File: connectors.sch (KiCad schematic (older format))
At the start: 43 parts, among them J11 20021121-00010C4LF, J12 70543-0001, J13 70543-0001, J14 70543-0001, J15 70543-0001, J16 70543-0001, J17 70543-0001, J18 70543-0001, J19 70543-0001, J20 70543-0003, J21 70543-0002, J22 70543-0002, J23 70543-0002, J24 Conn_02x20_Odd_Even

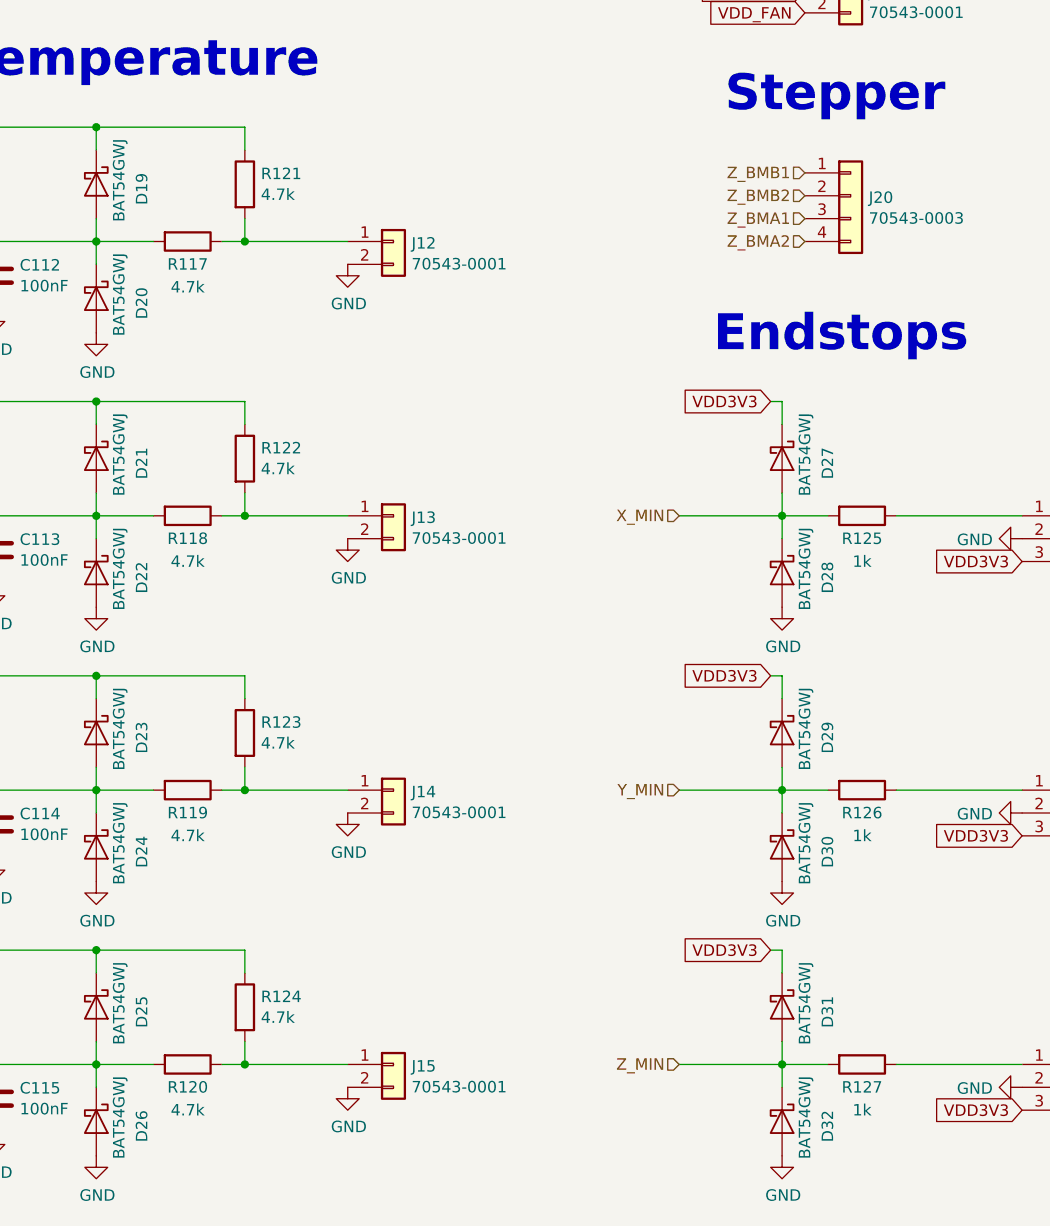
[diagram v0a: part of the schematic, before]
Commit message: Add transistor for boot selection
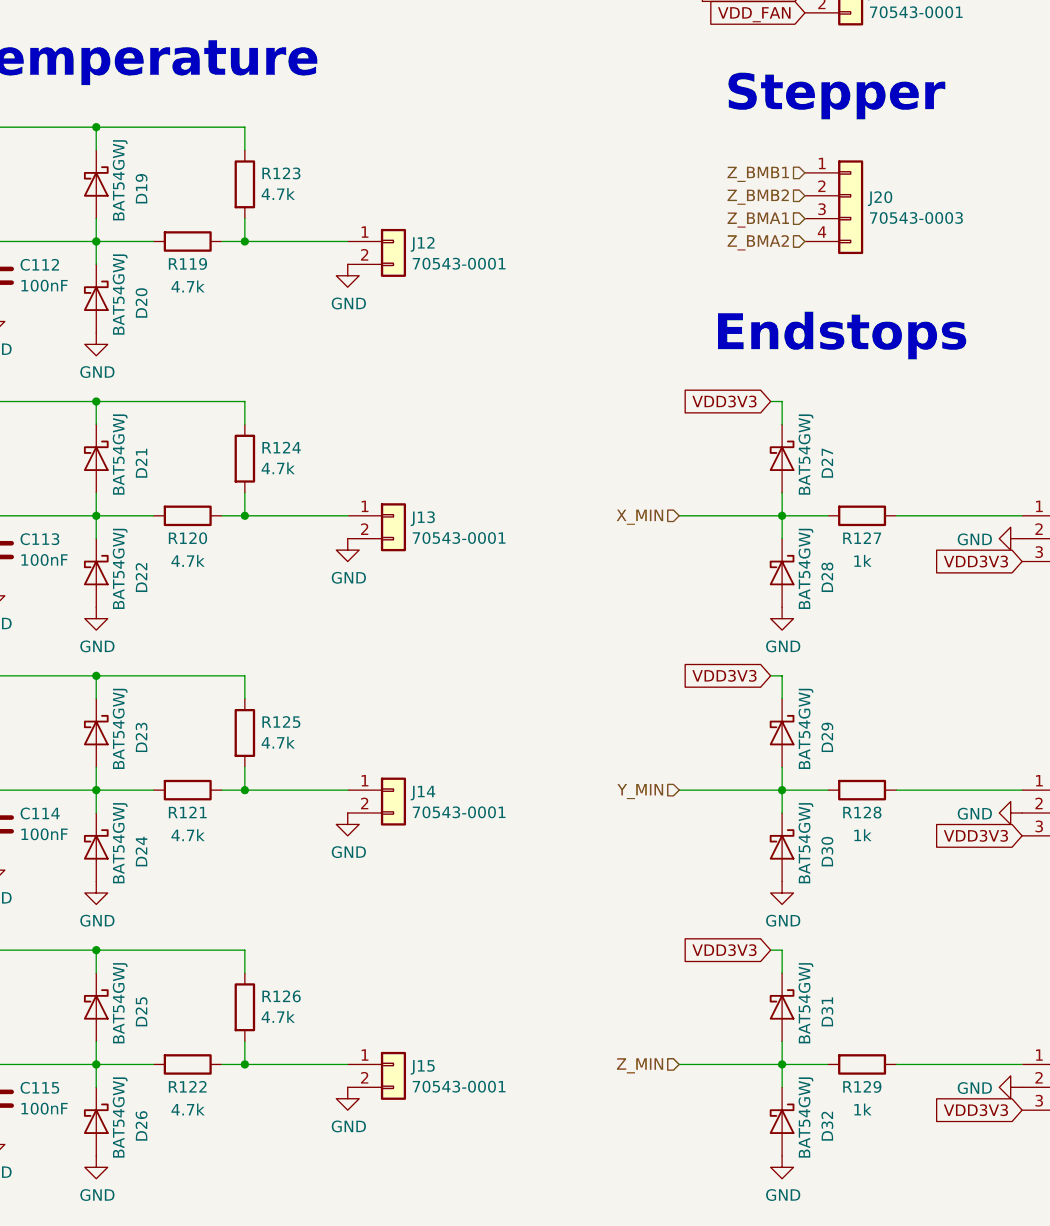
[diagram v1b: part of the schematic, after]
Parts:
- renumbered R117 to R119, R118 to R120, R119 to R121, R120 to R122, R121 to R123, R122 to R124, R123 to R125, R124 to R126, R125 to R127, R126 to R128, R127 to R129
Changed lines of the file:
@@
 TEMP1
 $Comp
-L Device:R R117
+L Device:R R119
 U 1 1 5B1719A1
 P 1900 3300
-F 0 "R117" V 2000 3300 50  0000 C CNN
+F 0 "R119" V 2000 3300 50  0000 C CNN
 F 1 "4.7k" V 2100 3300 50  0000 C CNN
 F 2 "Resistor_SMD:R_0603_1608Metric" V 1830 3300 50  0001 C CNN
@@
 $EndComp
 $Comp
-L Device:R R121
+L Device:R R123
 U 1 1 5B1719A8
 P 2150 3050
-F 0 "R121" H 2220 3096 50  0000 L CNN
+F 0 "R123" H 2220 3096 50  0000 L CNN
 F 1 "4.7k" H 2220 3005 50  0000 L CNN
 F 2 "Resistor_SMD:R_0603_1608Metric" V 2080 3050 50  0001 C CNN
@@
 VDD_FAN
 $Comp
-L Device:R R125
+L Device:R R127
 U 1 1 5B40FD8A
 P 4850 4500
-F 0 "R125" V 4950 4500 50  0000 C CNN
+F 0 "R127" V 4950 4500 50  0000 C CNN
 F 1 "1k" V 5050 4500 50  0000 C CNN
 F 2 "Resistor_SMD:R_0603_1608Metric" V 4780 4500 50  0001 C CNN
@@
 	4500 4500 4700 4500
 $Comp
-L Device:R R126
+L Device:R R128
 U 1 1 5B453619
 P 4850 5700
-F 0 "R126" V 4950 5700 50  0000 C CNN
+F 0 "R128" V 4950 5700 50  0000 C CNN
 F 1 "1k" V 5050 5700 50  0000 C CNN
 F 2 "Resistor_SMD:R_0603_1608Metric" V 4780 5700 50  0001 C CNN
@@
 	4500 5700 4700 5700
 $Comp
-L Device:R R127
+L Device:R R129
 U 1 1 5B45771E
 P 4850 6900
-F 0 "R127" V 4950 6900 50  0000 C CNN
+F 0 "R129" V 4950 6900 50  0000 C CNN
 F 1 "1k" V 5050 6900 50  0000 C CNN
 F 2 "Resistor_SMD:R_0603_1608Metric" V 4780 6900 50  0001 C CNN
@@
 Connection ~ 2150 3300
 $Comp
-L Device:R R118
+L Device:R R120
 U 1 1 5B5657F4
 P 1900 4500
-F 0 "R118" V 2000 4500 50  0000 C CNN
+F 0 "R120" V 2000 4500 50  0000 C CNN
 F 1 "4.7k" V 2100 4500 50  0000 C CNN
 F 2 "Resistor_SMD:R_0603_1608Metric" V 1830 4500 50  0001 C CNN
@@
 $EndComp
 $Comp
-L Device:R R122
+L Device:R R124
 U 1 1 5B5657FB
 P 2150 4250
-F 0 "R122" H 2220 4296 50  0000 L CNN
+F 0 "R124" H 2220 4296 50  0000 L CNN
 F 1 "4.7k" H 2220 4205 50  0000 L CNN
 F 2 "Resistor_SMD:R_0603_1608Metric" V 2080 4250 50  0001 C CNN
@@
 Connection ~ 2150 4500
 $Comp
-L Device:R R119
+L Device:R R121
 U 1 1 5B57C5BA
 P 1900 5700
-F 0 "R119" V 2000 5700 50  0000 C CNN
+F 0 "R121" V 2000 5700 50  0000 C CNN
 F 1 "4.7k" V 2100 5700 50  0000 C CNN
 F 2 "Resistor_SMD:R_0603_1608Metric" V 1830 5700 50  0001 C CNN
@@
 $EndComp
 $Comp
-L Device:R R123
+L Device:R R125
 U 1 1 5B57C5C1
 P 2150 5450
-F 0 "R123" H 2220 5496 50  0000 L CNN
+F 0 "R125" H 2220 5496 50  0000 L CNN
 F 1 "4.7k" H 2220 5405 50  0000 L CNN
 F 2 "Resistor_SMD:R_0603_1608Metric" V 2080 5450 50  0001 C CNN
@@
 $EndComp
 $Comp
-L Device:R R120
+L Device:R R122
 U 1 1 5BC983A7
 P 1900 6900
-F 0 "R120" V 2000 6900 50  0000 C CNN
+F 0 "R122" V 2000 6900 50  0000 C CNN
 F 1 "4.7k" V 2100 6900 50  0000 C CNN
 F 2 "Resistor_SMD:R_0603_1608Metric" V 1830 6900 50  0001 C CNN
@@
 $EndComp
 $Comp
-L Device:R R124
+L Device:R R126
 U 1 1 5BC983AE
 P 2150 6650
-F 0 "R124" H 2220 6696 50  0000 L CNN
+F 0 "R126" H 2220 6696 50  0000 L CNN
 F 1 "4.7k" H 2220 6605 50  0000 L CNN
 F 2 "Resistor_SMD:R_0603_1608Metric" V 2080 6650 50  0001 C CNN

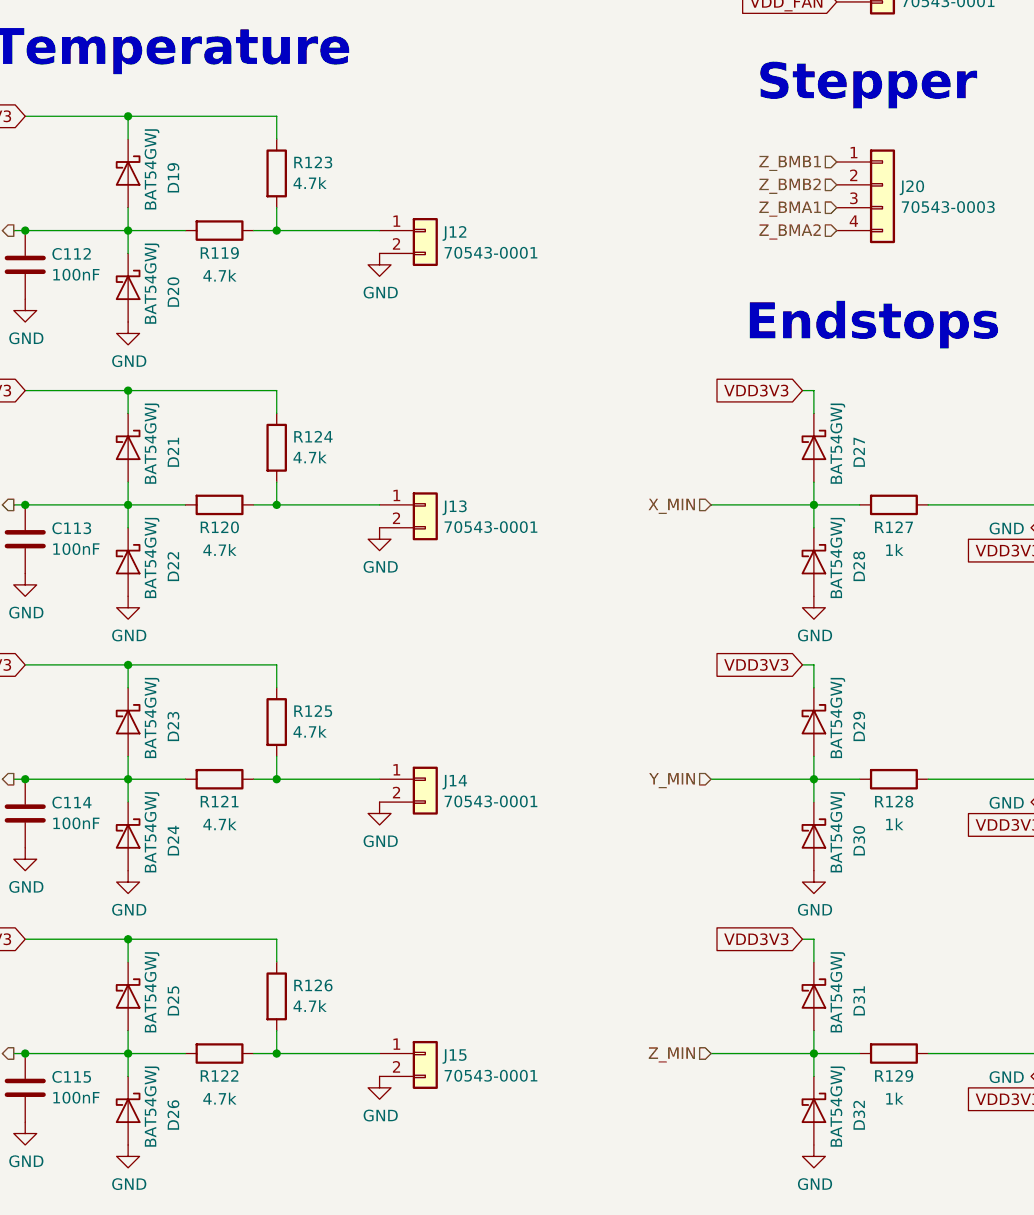
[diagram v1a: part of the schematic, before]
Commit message: Version 1.3
 * Changed to TH 100uF capacitators
 * Switched to SOT-23-3 MOSFETS
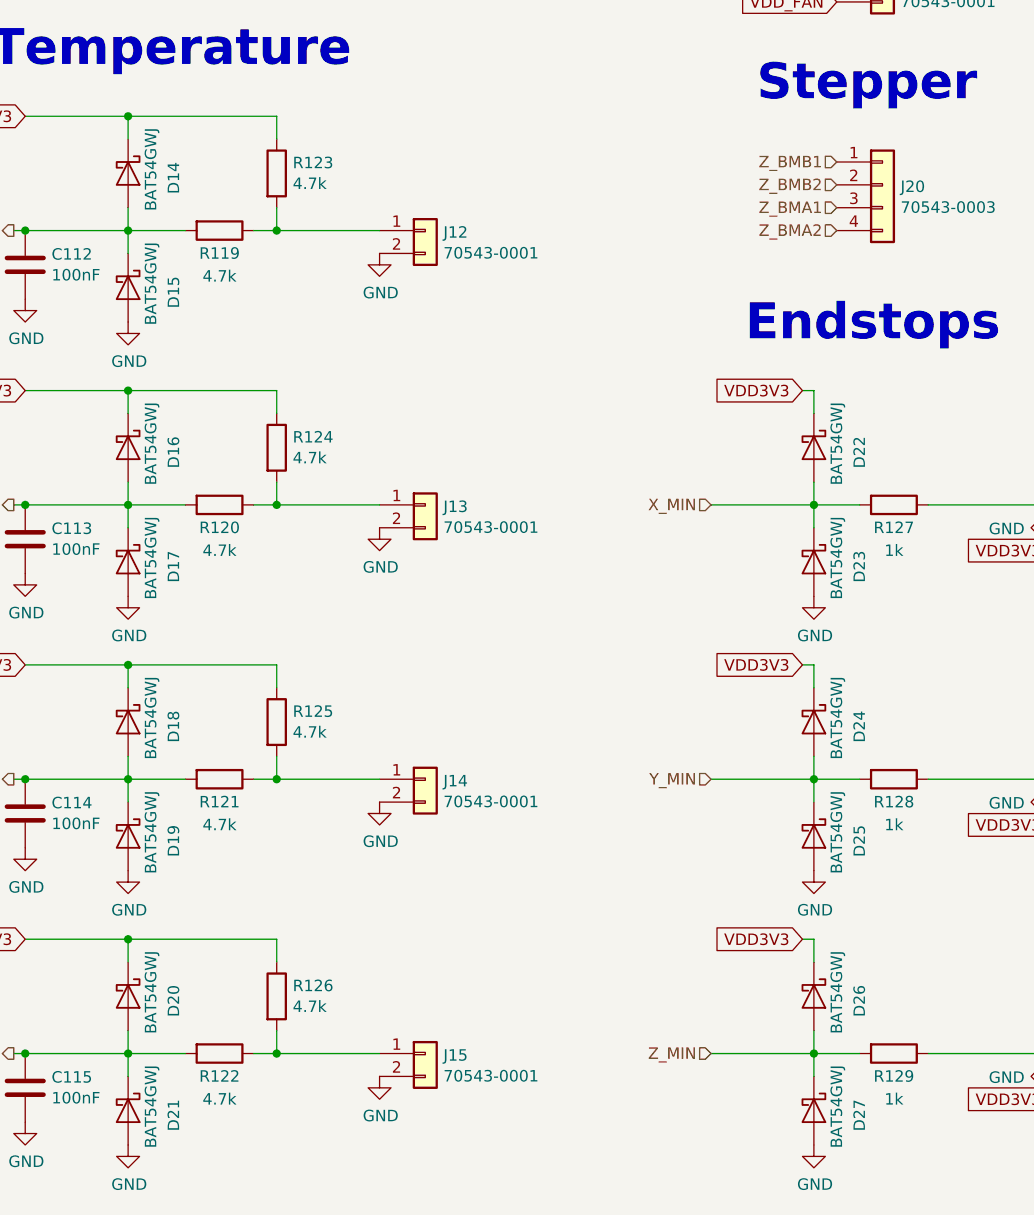
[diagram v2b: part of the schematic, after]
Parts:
- renumbered D19 to D14, D20 to D15, D21 to D16, D22 to D17, D23 to D18, D24 to D19, D25 to D20, D26 to D21, D27 to D22, D28 to D23, D29 to D24, D30 to D25, D31 to D26, D32 to D27
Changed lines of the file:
@@
 P 1500 3050
 AR Path="/5BC2F648/5BCF829E" Ref="D?"  Part="1"
-AR Path="/5BC2F290/5BCF829E" Ref="D19"  Part="1"
-F 0 "D19" H 1450 3250 50  0000 L CNN
+AR Path="/5BC2F290/5BCF829E" Ref="D14"  Part="1"
+F 0 "D14" H 1450 3250 50  0000 L CNN
 F 1 "BAT54GWJ" H 1300 3150 50  0000 L CNN
 F 2 "Diode_SMD:D_SOD-123" H 1500 3050 50  0001 C CNN
@@
 P 1500 4250
 AR Path="/5BC2F648/5BCFC008" Ref="D?"  Part="1"
-AR Path="/5BC2F290/5BCFC008" Ref="D21"  Part="1"
-F 0 "D21" H 1450 4450 50  0000 L CNN
+AR Path="/5BC2F290/5BCFC008" Ref="D16"  Part="1"
+F 0 "D16" H 1450 4450 50  0000 L CNN
 F 1 "BAT54GWJ" H 1300 4350 50  0000 L CNN
 F 2 "Diode_SMD:D_SOD-123" H 1500 4250 50  0001 C CNN
@@
 P 1500 4750
 AR Path="/5BC2F648/5BCFDE39" Ref="D?"  Part="1"
-AR Path="/5BC2F290/5BCFDE39" Ref="D22"  Part="1"
-F 0 "D22" H 1450 4950 50  0000 L CNN
+AR Path="/5BC2F290/5BCFDE39" Ref="D17"  Part="1"
+F 0 "D17" H 1450 4950 50  0000 L CNN
 F 1 "BAT54GWJ" H 1300 4850 50  0000 L CNN
 F 2 "Diode_SMD:D_SOD-123" H 1500 4750 50  0001 C CNN
@@
 P 1500 5450
 AR Path="/5BC2F648/5BCFFC64" Ref="D?"  Part="1"
-AR Path="/5BC2F290/5BCFFC64" Ref="D23"  Part="1"
-F 0 "D23" H 1450 5650 50  0000 L CNN
+AR Path="/5BC2F290/5BCFFC64" Ref="D18"  Part="1"
+F 0 "D18" H 1450 5650 50  0000 L CNN
 F 1 "BAT54GWJ" H 1300 5550 50  0000 L CNN
 F 2 "Diode_SMD:D_SOD-123" H 1500 5450 50  0001 C CNN
@@
 P 1500 5950
 AR Path="/5BC2F648/5BD01AAD" Ref="D?"  Part="1"
-AR Path="/5BC2F290/5BD01AAD" Ref="D24"  Part="1"
-F 0 "D24" H 1450 6150 50  0000 L CNN
+AR Path="/5BC2F290/5BD01AAD" Ref="D19"  Part="1"
+F 0 "D19" H 1450 6150 50  0000 L CNN
 F 1 "BAT54GWJ" H 1300 6050 50  0000 L CNN
 F 2 "Diode_SMD:D_SOD-123" H 1500 5950 50  0001 C CNN
@@
 P 1500 6650
 AR Path="/5BC2F648/5BD038E4" Ref="D?"  Part="1"
-AR Path="/5BC2F290/5BD038E4" Ref="D25"  Part="1"
-F 0 "D25" H 1450 6850 50  0000 L CNN
+AR Path="/5BC2F290/5BD038E4" Ref="D20"  Part="1"
+F 0 "D20" H 1450 6850 50  0000 L CNN
 F 1 "BAT54GWJ" H 1300 6750 50  0000 L CNN
 F 2 "Diode_SMD:D_SOD-123" H 1500 6650 50  0001 C CNN
@@
 P 1500 7150
 AR Path="/5BC2F648/5BD059B2" Ref="D?"  Part="1"
-AR Path="/5BC2F290/5BD059B2" Ref="D26"  Part="1"
-F 0 "D26" H 1450 7350 50  0000 L CNN
+AR Path="/5BC2F290/5BD059B2" Ref="D21"  Part="1"
+F 0 "D21" H 1450 7350 50  0000 L CNN
 F 1 "BAT54GWJ" H 1300 7250 50  0000 L CNN
 F 2 "Diode_SMD:D_SOD-123" H 1500 7150 50  0001 C CNN
@@
 P 4500 7150
 AR Path="/5BC2F648/5BD07803" Ref="D?"  Part="1"
-AR Path="/5BC2F290/5BD07803" Ref="D32"  Part="1"
-F 0 "D32" H 4450 7350 50  0000 L CNN
+AR Path="/5BC2F290/5BD07803" Ref="D27"  Part="1"
+F 0 "D27" H 4450 7350 50  0000 L CNN
 F 1 "BAT54GWJ" H 4300 7250 50  0000 L CNN
 F 2 "Diode_SMD:D_SOD-123" H 4500 7150 50  0001 C CNN
@@
 P 4500 6650
 AR Path="/5BC2F648/5BD09650" Ref="D?"  Part="1"
-AR Path="/5BC2F290/5BD09650" Ref="D31"  Part="1"
-F 0 "D31" H 4450 6850 50  0000 L CNN
+AR Path="/5BC2F290/5BD09650" Ref="D26"  Part="1"
+F 0 "D26" H 4450 6850 50  0000 L CNN
 F 1 "BAT54GWJ" H 4300 6750 50  0000 L CNN
 F 2 "Diode_SMD:D_SOD-123" H 4500 6650 50  0001 C CNN
@@
 P 4500 5950
 AR Path="/5BC2F648/5BD0B48B" Ref="D?"  Part="1"
-AR Path="/5BC2F290/5BD0B48B" Ref="D30"  Part="1"
-F 0 "D30" H 4450 6150 50  0000 L CNN
+AR Path="/5BC2F290/5BD0B48B" Ref="D25"  Part="1"
+F 0 "D25" H 4450 6150 50  0000 L CNN
 F 1 "BAT54GWJ" H 4300 6050 50  0000 L CNN
 F 2 "Diode_SMD:D_SOD-123" H 4500 5950 50  0001 C CNN
@@
 P 4500 4750
 AR Path="/5BC2F648/5BD0D2CE" Ref="D?"  Part="1"
-AR Path="/5BC2F290/5BD0D2CE" Ref="D28"  Part="1"
-F 0 "D28" H 4450 4950 50  0000 L CNN
+AR Path="/5BC2F290/5BD0D2CE" Ref="D23"  Part="1"
+F 0 "D23" H 4450 4950 50  0000 L CNN
 F 1 "BAT54GWJ" H 4300 4850 50  0000 L CNN
 F 2 "Diode_SMD:D_SOD-123" H 4500 4750 50  0001 C CNN
@@
 P 4500 4250
 AR Path="/5BC2F648/5BD0F10B" Ref="D?"  Part="1"
-AR Path="/5BC2F290/5BD0F10B" Ref="D27"  Part="1"
-F 0 "D27" H 4450 4450 50  0000 L CNN
+AR Path="/5BC2F290/5BD0F10B" Ref="D22"  Part="1"
+F 0 "D22" H 4450 4450 50  0000 L CNN
 F 1 "BAT54GWJ" H 4300 4350 50  0000 L CNN
 F 2 "Diode_SMD:D_SOD-123" H 4500 4250 50  0001 C CNN
@@
 P 4500 5450
 AR Path="/5BC2F648/5BD10F46" Ref="D?"  Part="1"
-AR Path="/5BC2F290/5BD10F46" Ref="D29"  Part="1"
-F 0 "D29" H 4450 5650 50  0000 L CNN
+AR Path="/5BC2F290/5BD10F46" Ref="D24"  Part="1"
+F 0 "D24" H 4450 5650 50  0000 L CNN
 F 1 "BAT54GWJ" H 4300 5550 50  0000 L CNN
 F 2 "Diode_SMD:D_SOD-123" H 4500 5450 50  0001 C CNN
@@
 P 1500 3550
 AR Path="/5BC2F648/5BD130B1" Ref="D?"  Part="1"
-AR Path="/5BC2F290/5BD130B1" Ref="D20"  Part="1"
-F 0 "D20" H 1450 3750 50  0000 L CNN
+AR Path="/5BC2F290/5BD130B1" Ref="D15"  Part="1"
+F 0 "D15" H 1450 3750 50  0000 L CNN
 F 1 "BAT54GWJ" H 1300 3650 50  0000 L CNN
 F 2 "Diode_SMD:D_SOD-123" H 1500 3550 50  0001 C CNN
